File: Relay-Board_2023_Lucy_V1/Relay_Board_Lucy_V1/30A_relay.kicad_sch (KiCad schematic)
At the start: 1 part, among them K4 PTRH-1C-12S-1-X

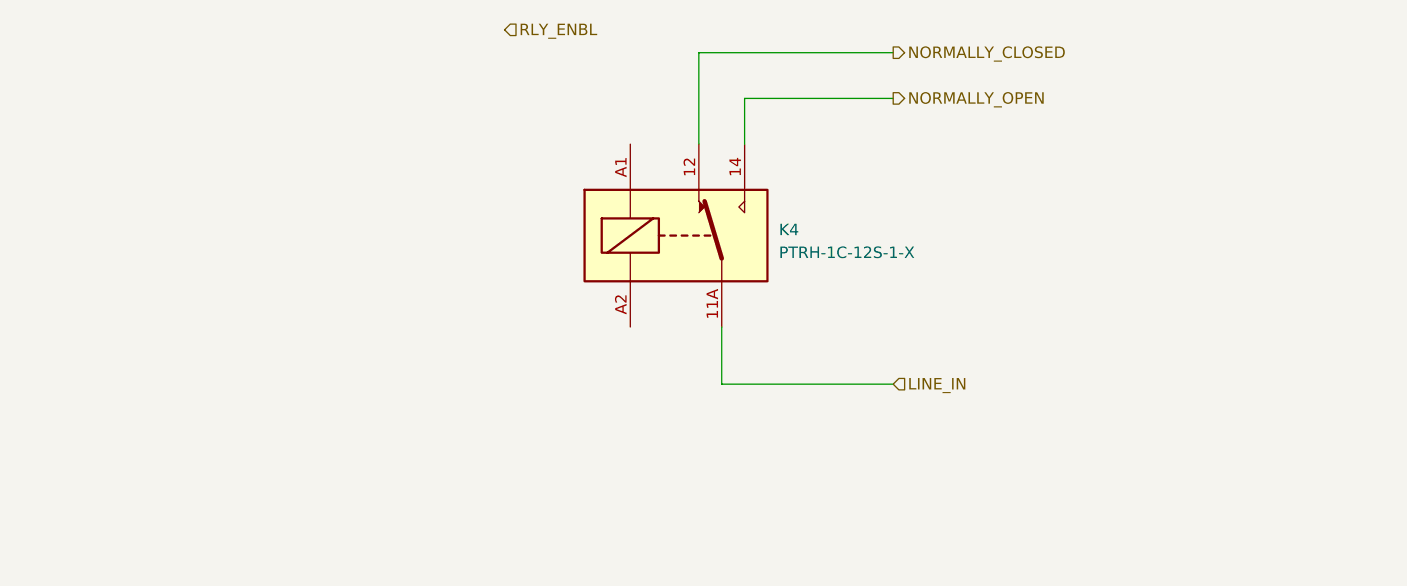
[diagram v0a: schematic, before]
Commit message: Added uart to usb, still needs some work, started prog for mcu
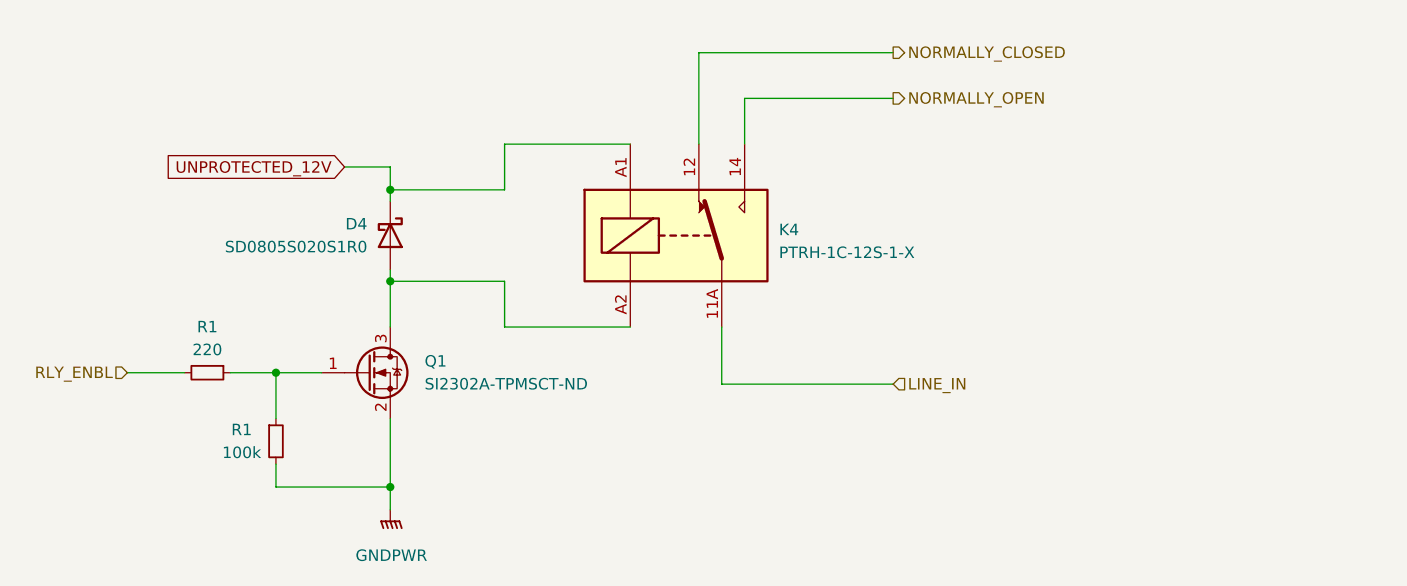
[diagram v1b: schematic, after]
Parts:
- added D4: SD0805S020S1R0, Diode_SMD:D_0805_2012Metric_Pad1.15x1.40mm_HandSolder, symbol Device:D_Schottky
- added Q1: SI2302A-TPMSCT-ND, Package_TO_SOT_SMD:SOT-23-3, symbol Device:Q_NMOS_GSD
- added R1: 220, symbol Device:R_Small
- added R1: 100k, symbol Device:R_Small
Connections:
- net RLY_ENBL: now also R1.2
- net UNPROTECTED_12V: now reaches K4.A1
- net UNPROTECTED_12V: now also D4.1 (K)
- net at K4.A2: now also D4.2 (A), Q1.3 (D)
- new net: Q1.1 (G), R1.1, R1.1
- new net GNDPWR: Q1.2 (S), R1.2

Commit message: lots of big changes
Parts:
- renumbered D4 to D5
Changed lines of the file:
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@@
   (symbol (lib_id "power:GNDPWR") (at 114.3 127 0) (mirror y) (unit 1)
     (in_bom yes) (on_board yes) (dnp no) (fields_autoplaced)
-    (property "Reference" "#PWR018" (at 114.3 132.08 0)
+    (property "Reference" "#PWR020" (at 114.3 132.08 0)
       (effects (font (size 1.27 1.27)) hide)
     )
@@
     (instances
       (project "Relay_Board_Lucy_V1"
-        (path "/1f586fab-d165-4cda-895e-cc224a8182b4/dd97e156-5589-4023-8217-f04bbcc4a9fe"
-          (reference "#PWR018") (unit 1)
-        )
         (path "/1f586fab-d165-4cda-895e-cc224a8182b4/e3e3a679-5f79-4d77-8bec-4f63930827cc"
           (reference "#PWR020") (unit 1)
@@
     )
     (property "Datasheet" "https://pickercomponents.com/pdf/Relays/PTRH.pdf" (at 146.05 96.52 0)
+      (effects (font (size 1.27 1.27)) hide)
+    )
+    (property "Part#" "" (at 146.05 96.52 0)
       (effects (font (size 1.27 1.27)) hide)
     )
@@
       (effects (font (size 1.27 1.27)) hide)
     )
+    (property "Part#" "" (at 93.98 111.76 0)
+      (effects (font (size 1.27 1.27)) hide)
+    )
     (pin "1")
     (pin "2")
@@
         (path "/1f586fab-d165-4cda-895e-cc224a8182b4"
           (reference "R2") (unit 1)
-        )
-        (path "/1f586fab-d165-4cda-895e-cc224a8182b4/dd97e156-5589-4023-8217-f04bbcc4a9fe"
-          (reference "R10") (unit 1)
         )
         (path "/1f586fab-d165-4cda-895e-cc224a8182b4/e3e3a679-5f79-4d77-8bec-4f63930827cc"
@@
       (effects (font (size 1.27 1.27)) hide)
     )
+    (property "Part#" "" (at 111.76 111.76 0)
+      (effects (font (size 1.27 1.27)) hide)
+    )
     (pin "1")
     (pin "2")
@@
         (path "/1f586fab-d165-4cda-895e-cc224a8182b4"
           (reference "Q1") (unit 1)
-        )
-        (path "/1f586fab-d165-4cda-895e-cc224a8182b4/dd97e156-5589-4023-8217-f04bbcc4a9fe"
-          (reference "Q2") (unit 1)
         )
         (path "/1f586fab-d165-4cda-895e-cc224a8182b4/e3e3a679-5f79-4d77-8bec-4f63930827cc"
@@
   (symbol (lib_id "Device:D_Schottky") (at 114.3 96.52 270) (unit 1)
     (in_bom yes) (on_board yes) (dnp no)
-    (property "Reference" "D4" (at 111.76 95.25 90)
+    (property "Reference" "D5" (at 111.76 95.25 90)
       (effects (font (size 1.27 1.27)) (justify right))
     )
@@
       (effects (font (size 1.27 1.27)) hide)
     )
-    (pin "1")
-    (pin "2")
-    (instances
-      (project "Relay_Board_Lucy_V1"
-        (path "/1f586fab-d165-4cda-895e-cc224a8182b4/dd97e156-5589-4023-8217-f04bbcc4a9fe"
-          (reference "D4") (unit 1)
-        )
+    (property "Part#" "" (at 114.3 96.52 0)
+      (effects (font (size 1.27 1.27)) hide)
+    )
+    (pin "1")
+    (pin "2")
+    (instances
+      (project "Relay_Board_Lucy_V1"
         (path "/1f586fab-d165-4cda-895e-cc224a8182b4/e3e3a679-5f79-4d77-8bec-4f63930827cc"
           (reference "D5") (unit 1)
@@
       (effects (font (size 1.27 1.27)) hide)
     )
+    (property "Part#" "" (at 101.6 119.38 0)
+      (effects (font (size 1.27 1.27)) hide)
+    )
     (pin "1")
     (pin "2")
@@
           (reference "R2") (unit 1)
         )
-        (path "/1f586fab-d165-4cda-895e-cc224a8182b4/dd97e156-5589-4023-8217-f04bbcc4a9fe"
-          (reference "R13") (unit 1)
-        )
-        (path "/1f586fab-d165-4cda-895e-cc224a8182b4/e3e3a679-5f79-4d77-8bec-4f63930827cc"
+        (path "/1f586fab-d165-4cda-895e-cc224a8182b4/e3e3a679-5f79-4d77-8bec-4f63930827cc"

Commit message: Updates
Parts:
- R1: footprint (none) -> Resistor_SMD:R_0603_1608Metric
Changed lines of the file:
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@@
         )
         (path "/1f586fab-d165-4cda-895e-cc224a8182b4/ed81dffe-8ef6-4a6b-bb11-de534fb08671"
-          (reference "#PWR022") (unit 1)
-        )
-        (path "/1f586fab-d165-4cda-895e-cc224a8182b4/4b1c0f83-d3c7-42cf-a2fc-f90e1b4570a4"
-          (reference "#PWR046") (unit 1)
+          (reference "#PWR065") (unit 1)
+        )
+        (path "/1f586fab-d165-4cda-895e-cc224a8182b4/4b1c0f83-d3c7-42cf-a2fc-f90e1b4570a4"
+          (reference "#PWR066") (unit 1)
         )
       )
@@
         )
         (path "/1f586fab-d165-4cda-895e-cc224a8182b4/ed81dffe-8ef6-4a6b-bb11-de534fb08671"
-          (reference "K6") (unit 1)
+          (reference "K3") (unit 1)
         )
         (path "/1f586fab-d165-4cda-895e-cc224a8182b4/4b1c0f83-d3c7-42cf-a2fc-f90e1b4570a4"
@@
       (effects (font (size 1.27 1.27)))
     )
-    (property "Footprint" "" (at 93.98 111.76 0)
+    (property "Footprint" "Resistor_SMD:R_0603_1608Metric" (at 93.98 111.76 0)
       (effects (font (size 1.27 1.27)) hide)
     )
@@
         )
         (path "/1f586fab-d165-4cda-895e-cc224a8182b4/ed81dffe-8ef6-4a6b-bb11-de534fb08671"
-          (reference "R17") (unit 1)
-        )
-        (path "/1f586fab-d165-4cda-895e-cc224a8182b4/4b1c0f83-d3c7-42cf-a2fc-f90e1b4570a4"
-          (reference "R19") (unit 1)
+          (reference "R30") (unit 1)
+        )
+        (path "/1f586fab-d165-4cda-895e-cc224a8182b4/4b1c0f83-d3c7-42cf-a2fc-f90e1b4570a4"
+          (reference "R32") (unit 1)
         )
       )
@@
         )
         (path "/1f586fab-d165-4cda-895e-cc224a8182b4/ed81dffe-8ef6-4a6b-bb11-de534fb08671"
+          (reference "Q4") (unit 1)
+        )
+        (path "/1f586fab-d165-4cda-895e-cc224a8182b4/4b1c0f83-d3c7-42cf-a2fc-f90e1b4570a4"
           (reference "Q5") (unit 1)
-        )
-        (path "/1f586fab-d165-4cda-895e-cc224a8182b4/4b1c0f83-d3c7-42cf-a2fc-f90e1b4570a4"
-          (reference "Q6") (unit 1)
         )
       )
@@
         )
         (path "/1f586fab-d165-4cda-895e-cc224a8182b4/ed81dffe-8ef6-4a6b-bb11-de534fb08671"
-          (reference "D9") (unit 1)
-        )
-        (path "/1f586fab-d165-4cda-895e-cc224a8182b4/4b1c0f83-d3c7-42cf-a2fc-f90e1b4570a4"
-          (reference "D10") (unit 1)
+          (reference "D14") (unit 1)
+        )
+        (path "/1f586fab-d165-4cda-895e-cc224a8182b4/4b1c0f83-d3c7-42cf-a2fc-f90e1b4570a4"
+          (reference "D15") (unit 1)
         )
       )
@@
       (effects (font (size 1.27 1.27)))
     )
-    (property "Footprint" "" (at 101.6 119.38 0)
+    (property "Footprint" "Resistor_SMD:R_0603_1608Metric" (at 101.6 119.38 0)
       (effects (font (size 1.27 1.27)) hide)
     )
@@
         )
         (path "/1f586fab-d165-4cda-895e-cc224a8182b4/ed81dffe-8ef6-4a6b-bb11-de534fb08671"
-          (reference "R16") (unit 1)
-        )
-        (path "/1f586fab-d165-4cda-895e-cc224a8182b4/4b1c0f83-d3c7-42cf-a2fc-f90e1b4570a4"
-          (reference "R18") (unit 1)
-        )
-      )
+          (reference "R31") (unit 1)
+        )
+        (path "/1f586fab-d165-4cda-895e-cc224a8182b4/4b1c0f83-d3c7-42cf-a2fc-f90e1b4570a4"
+          (reference "R33") (unit 1)
+        )
+      )

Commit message: Started the PCB design work
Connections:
- net GNDPWR renamed GNDA
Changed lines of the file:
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@@
     (effects (font (size 1.27 1.27)) (justify left))
-  )
-  (symbol (lib_id "power:GNDPWR") (at 114.3 127 0) (mirror y) (unit 1)
-    (in_bom yes) (on_board yes) (dnp no) (fields_autoplaced)
-    (property "Reference" "#PWR020" (at 114.3 132.08 0)
-      (effects (font (size 1.27 1.27)) hide)
-    )
-    (property "Value" "GNDPWR" (at 114.427 132.08 0)
-      (effects (font (size 1.27 1.27)))
-    )
-    (property "Footprint" "" (at 114.3 128.27 0)
-      (effects (font (size 1.27 1.27)) hide)
-    )
-    (property "Datasheet" "" (at 114.3 128.27 0)
-      (effects (font (size 1.27 1.27)) hide)
-    )
-    (pin "1")
-    (instances
-      (project "Relay_Board_Lucy_V1"
-        (path "/1f586fab-d165-4cda-895e-cc224a8182b4/e3e3a679-5f79-4d77-8bec-4f63930827cc"
-          (reference "#PWR020") (unit 1)
-        )
-        (path "/1f586fab-d165-4cda-895e-cc224a8182b4/2c5921d2-6c17-4365-bb30-821f28165af3"
-          (reference "#PWR021") (unit 1)
-        )
-        (path "/1f586fab-d165-4cda-895e-cc224a8182b4/ed81dffe-8ef6-4a6b-bb11-de534fb08671"
-          (reference "#PWR065") (unit 1)
-        )
-        (path "/1f586fab-d165-4cda-895e-cc224a8182b4/4b1c0f83-d3c7-42cf-a2fc-f90e1b4570a4"
-          (reference "#PWR066") (unit 1)
-        )
-      )
-    )
   )
   (symbol (lib_id "RB_PARTS:PTRH-1C-12S-1-X") (at 146.05 96.52 0) (unit 1)
@@
         )
       )
+    )
+  )
+  (symbol (lib_id "power:GNDA") (at 114.3 127 0) (unit 1)
+    (in_bom yes) (on_board yes) (dnp no)
+    (property "Reference" "#PWR023" (at 114.3 133.35 0)
+      (effects (font (size 1.27 1.27)) hide)
+    )
+    (property "Value" "GNDA" (at 116.84 132.08 0)
+      (effects (font (size 1.27 1.27)) (justify right))
+    )
+    (property "Footprint" "" (at 114.3 127 0)
+      (effects (font (size 1.27 1.27)) hide)
+    )
+    (property "Datasheet" "" (at 114.3 127 0)
+      (effects (font (size 1.27 1.27)) hide)
+    )
+    (pin "1")
+    (instances
+      (project "Relay_Board_Lucy_V1"
+        (path "/1f586fab-d165-4cda-895e-cc224a8182b4/d0430468-7d1b-42a2-a24e-658bd737b804"
+          (reference "#PWR023") (unit 1)
+        )
+        (path "/1f586fab-d165-4cda-895e-cc224a8182b4"
+          (reference "#PWR025") (unit 1)
+        )
+        (path "/1f586fab-d165-4cda-895e-cc224a8182b4/ed81dffe-8ef6-4a6b-bb11-de534fb08671"
+          (reference "#PWR05") (unit 1)
+        )
+        (path "/1f586fab-d165-4cda-895e-cc224a8182b4/4b1c0f83-d3c7-42cf-a2fc-f90e1b4570a4"
+          (reference "#PWR028") (unit 1)
+        )
+      )

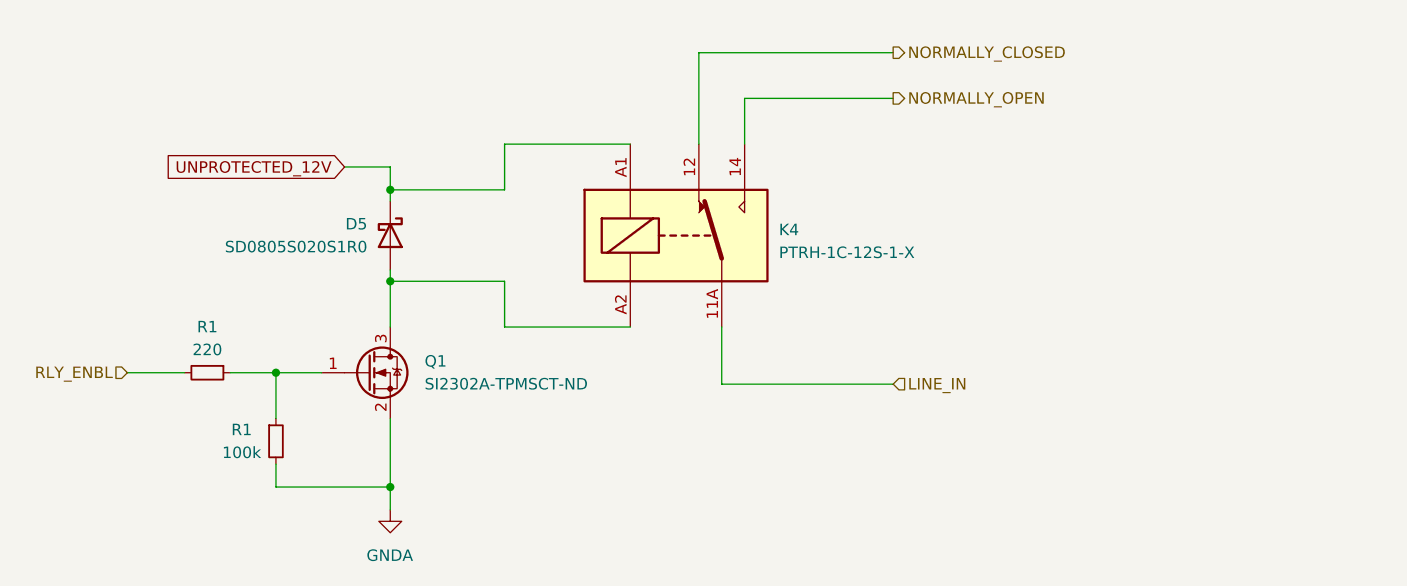
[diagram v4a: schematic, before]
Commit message: Finished the relay board. Once gerbers and drill files are generated we can order from jlc
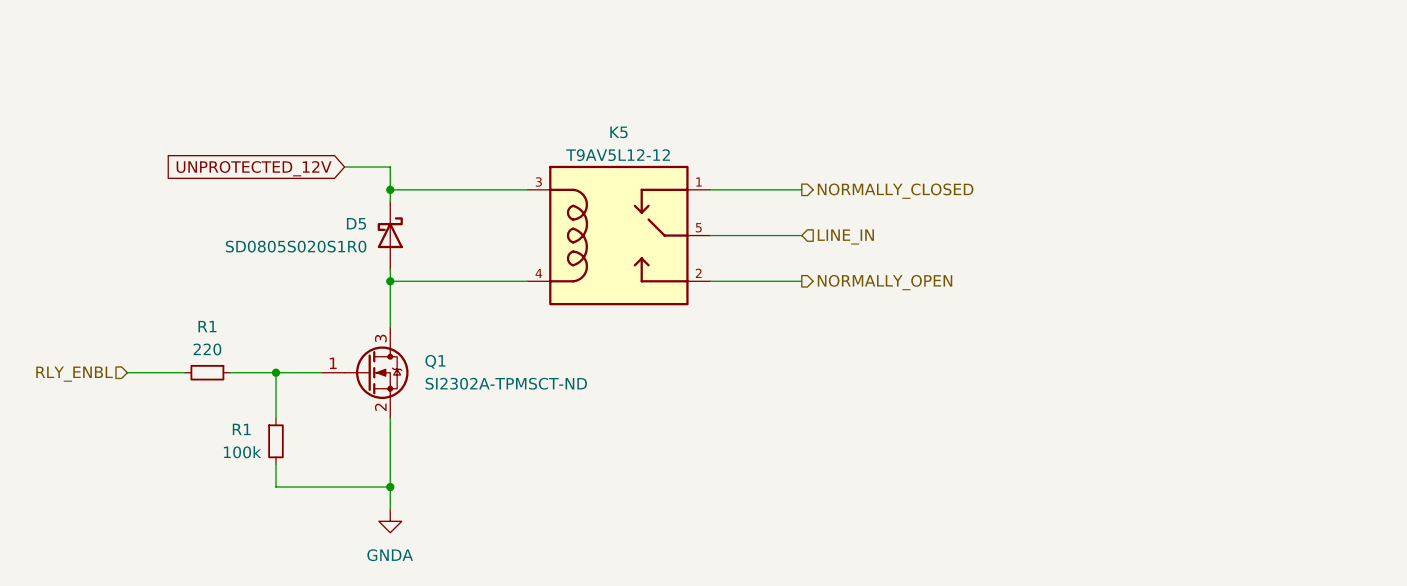
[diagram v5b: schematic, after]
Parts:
- removed K4: PTRH-1C-12S-1-X, RB_FTP:PTRH-1C-12S-1-X, symbol RB_PARTS:PTRH-1C-12S-1-X
- added K5: T9AV5L12-12, RB_FTP:T9AV5L12-12, symbol RB_PARTS:T9AV5L12-12
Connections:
- net LINE_IN: now also K5.5
- net NORMALLY_CLOSED: now also K5.1
- net NORMALLY_OPEN: now also K5.2
- net UNPROTECTED_12V: now also K5.3
- net at D5.2 (A), Q1.3 (D): now also K5.4
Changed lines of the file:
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@@
   (junction (at 101.6 111.76) (diameter 0) (color 0 0 0 0)
   )
-  (wire (pts (xy 148.59 76.2) (xy 170.18 76.2))
+  (wire (pts (xy 149.86 91.44) (xy 160.02 91.44))
     (stroke (width 0) (type default))
   )
-  (wire (pts (xy 114.3 91.44) (xy 127 91.44))
+  (wire (pts (xy 114.3 91.44) (xy 129.54 91.44))
     (stroke (width 0) (type default))
   )
@@
     (stroke (width 0) (type default))
   )
-  (wire (pts (xy 140.97 106.68) (xy 127 106.68))
+  (wire (pts (xy 114.3 101.6) (xy 129.54 101.6))
     (stroke (width 0) (type default))
   )
   (wire (pts (xy 114.3 88.9) (xy 114.3 91.44))
-    (stroke (width 0) (type default))
-  )
-  (wire (pts (xy 148.59 86.36) (xy 148.59 76.2))
-    (stroke (width 0) (type default))
-  )
-  (wire (pts (xy 153.67 86.36) (xy 153.67 81.28))
     (stroke (width 0) (type default))
   )
@@
     (stroke (width 0) (type default))
   )
-  (wire (pts (xy 127 106.68) (xy 127 101.6))
-    (stroke (width 0) (type default))
-  )
   (wire (pts (xy 114.3 124.46) (xy 114.3 127))
     (stroke (width 0) (type default))
@@
     (stroke (width 0) (type default))
   )
-  (wire (pts (xy 151.13 106.68) (xy 151.13 113.03))
-    (stroke (width 0) (type default))
-  )
-  (wire (pts (xy 127 91.44) (xy 127 86.36))
-    (stroke (width 0) (type default))
-  )
   (wire (pts (xy 101.6 111.76) (xy 106.68 111.76))
     (stroke (width 0) (type default))
   )
-  (wire (pts (xy 151.13 113.03) (xy 170.18 113.03))
+  (wire (pts (xy 149.86 96.52) (xy 160.02 96.52))
     (stroke (width 0) (type default))
   )
-  (wire (pts (xy 127 86.36) (xy 140.97 86.36))
+  (wire (pts (xy 149.86 101.6) (xy 160.02 101.6))
     (stroke (width 0) (type default))
   )
   (wire (pts (xy 96.52 111.76) (xy 101.6 111.76))
-    (stroke (width 0) (type default))
-  )
-  (wire (pts (xy 153.67 81.28) (xy 170.18 81.28))
     (stroke (width 0) (type default))
   )
@@
   )
   (wire (pts (xy 114.3 101.6) (xy 114.3 106.68))
-    (stroke (width 0) (type default))
-  )
-  (wire (pts (xy 114.3 101.6) (xy 127 101.6))
     (stroke (width 0) (type default))
   )
@@
     (effects (font (size 1.27 1.27)) (justify right))
   )
-  (hierarchical_label "LINE_IN" (shape input) (at 170.18 113.03 0) (fields_autoplaced)
+  (hierarchical_label "LINE_IN" (shape input) (at 160.02 96.52 0) (fields_autoplaced)
     (effects (font (size 1.27 1.27)) (justify left))
   )
-  (hierarchical_label "NORMALLY_OPEN" (shape output) (at 170.18 81.28 0) (fields_autoplaced)
+  (hierarchical_label "NORMALLY_OPEN" (shape output) (at 160.02 101.6 0) (fields_autoplaced)
     (effects (font (size 1.27 1.27)) (justify left))
   )
-  (hierarchical_label "NORMALLY_CLOSED" (shape output) (at 170.18 76.2 0) (fields_autoplaced)
+  (hierarchical_label "NORMALLY_CLOSED" (shape output) (at 160.02 91.44 0) (fields_autoplaced)
     (effects (font (size 1.27 1.27)) (justify left))
-  )
-  (symbol (lib_id "RB_PARTS:PTRH-1C-12S-1-X") (at 146.05 96.52 0) (unit 1)
-    (in_bom yes) (on_board yes) (dnp no) (fields_autoplaced)
-    (property "Reference" "K4" (at 157.48 95.885 0)
-      (effects (font (size 1.27 1.27)) (justify left))
-    )
-    (property "Value" "PTRH-1C-12S-1-X" (at 157.48 98.425 0)
-      (effects (font (size 1.27 1.27)) (justify left))
-    )
-    (property "Footprint" "RB_FTP:PTRH-1C-12S-1-X" (at 146.05 96.52 0)
-      (effects (font (size 1.27 1.27)) hide)
-    )
-    (property "Datasheet" "https://pickercomponents.com/pdf/Relays/PTRH.pdf" (at 146.05 96.52 0)
-      (effects (font (size 1.27 1.27)) hide)
-    )
-    (property "Part#" "" (at 146.05 96.52 0)
-      (effects (font (size 1.27 1.27)) hide)
-    )
-    (pin "11A")
-    (pin "11B")
-    (pin "12")
-    (pin "14")
-    (pin "A1")
-    (pin "A2")
-    (instances
-      (project "Relay_Board_Lucy_V1"
-        (path "/1f586fab-d165-4cda-895e-cc224a8182b4"
-          (reference "K4") (unit 1)
-        )
-        (path "/1f586fab-d165-4cda-895e-cc224a8182b4/ed81dffe-8ef6-4a6b-bb11-de534fb08671"
-          (reference "K3") (unit 1)
-        )
-        (path "/1f586fab-d165-4cda-895e-cc224a8182b4/4b1c0f83-d3c7-42cf-a2fc-f90e1b4570a4"
-          (reference "K4") (unit 1)
-        )
-      )
-    )
   )
   (symbol (lib_id "power:GNDA") (at 114.3 127 0) (unit 1)
@@
         )
       )
+    )
+  )
+  (symbol (lib_id "RB_PARTS:T9AV5L12-12") (at 139.7 96.52 0) (unit 1)
+    (in_bom yes) (on_board yes) (dnp no) (fields_autoplaced)
+    (property "Reference" "K5" (at 139.7 85.09 0)
+      (effects (font (size 1.27 1.27)))
+    )
+    (property "Value" "T9AV5L12-12" (at 139.7 87.63 0)
+      (effects (font (size 1.27 1.27)))
+    )
+    (property "Footprint" "RB_FTP:T9AV5L12-12" (at 139.7 96.52 0)
+      (effects (font (size 1.27 1.27)) (justify bottom) hide)
+    )
+    (property "Datasheet" "http://www.te.com/commerce/DocumentDelivery/DDEController?Action=showdoc&DocId=Data+Sheet%7F1308242_T9A%7F0915%7Fpdf%7FEnglish%7FENG_DS_1308242_T9A_0915.pdf%7F1423091-6" (at 139.7 109.22 0)
+      (effects (font (size 1.27 1.27)) hide)
+    )
+    (pin "1")
+    (pin "2")
+    (pin "3")
+    (pin "4")
+    (pin "5")
+    (instances
+      (project "Relay_Board_Lucy_V1"
+        (path "/1f586fab-d165-4cda-895e-cc224a8182b4"
+          (reference "K5") (unit 1)
+        )
+        (path "/1f586fab-d165-4cda-895e-cc224a8182b4/ed81dffe-8ef6-4a6b-bb11-de534fb08671"
+          (reference "K4") (unit 1)
+        )
+        (path "/1f586fab-d165-4cda-895e-cc224a8182b4/4b1c0f83-d3c7-42cf-a2fc-f90e1b4570a4"
+          (reference "K3") (unit 1)
+        )
+      )
